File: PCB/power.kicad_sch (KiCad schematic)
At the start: 59 parts, among them CON1 AVR-JTAG-10, U1 LM3880, U2 LM3880, U20 xc7z020clg484, U3 SC189 - 1.0V, U4 SC189 - 3.3V, U5 TLV62080DSGx, U7 SC189 - 1.8V

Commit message: Resolved most of the errors
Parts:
- added J401: Conn_01x02, Connector_PinSocket_1.00mm:PinSocket_1x02_P1.00mm_Vertical, symbol Connector_Generic:Conn_01x02
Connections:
- net +5V: now also J401.1 (Pin_1)
- net GND: now also J401.2 (Pin_2)
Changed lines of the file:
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@@
+	(symbol
+		(lib_id "DFTBoard-rescue:+5V-power")
+		(at 153.67 52.07 0)
+		(unit 1)
+		(exclude_from_sim no)
+		(in_bom yes)
+		(on_board yes)
+		(dnp no)
+		(property "Reference" "#PWR0402"
+			(at 153.67 49.784 0)
+			(effects
+				(font
+					(size 0.508 0.508)
+				)
+				(hide yes)
+			)
+		)
+		(property "Value" "+5V"
+			(at 153.67 49.784 0)
+			(effects
+				(font
+					(size 0.762 0.762)
+				)
+			)
+		)
+		(property "Footprint" ""
+			(at 153.67 52.07 0)
+			(effects
+				(font
+					(size 1.524 1.524)
+				)
+				(hide yes)
+			)
+		)
+		(property "Datasheet" ""
+			(at 153.67 52.07 0)
+			(effects
+				(font
+					(size 1.524 1.524)
+				)
+				(hide yes)
+			)
+		)
+		(property "Description" ""
+			(at 153.67 52.07 0)
+			(effects
+				(font
+					(size 1.27 1.27)
+				)
+				(hide yes)
+			)
+		)
+		(pin "1"
+		)
+		(instances
+			(project "DFTBoard"
+				(path "/0cf42e13-7c72-4f5f-898b-a3f851b94890/00000000-0000-0000-0000-000058508414"
+					(reference "#PWR0402")
+					(unit 1)
+				)
+			)
+		)
+	)
 	(symbol
 		(lib_id "DFTBoard-rescue:+5V-power")
@@
 					(unit 1)
 				)
+			)
+		)
+	)
+	(symbol
+		(lib_id "DFTBoard-rescue:GND-power")
+		(at 153.67 54.61 0)
+		(unit 1)
+		(exclude_from_sim no)
+		(in_bom yes)
+		(on_board yes)
+		(dnp no)
+		(property "Reference" "#PWR0403"
+			(at 153.67 54.61 0)
+			(effects
+				(font
+					(size 0.762 0.762)
+				)
+				(hide yes)
+			)
+		)
+		(property "Value" "GND"
+			(at 153.67 56.388 0)
+			(effects
+				(font
+					(size 0.762 0.762)
+				)
+				(hide yes)
+			)
+		)
+		(property "Footprint" ""
+			(at 153.67 54.61 0)
+			(effects
+				(font
+					(size 1.524 1.524)
+				)
+				(hide yes)
+			)
+		)
+		(property "Datasheet" ""
+			(at 153.67 54.61 0)
+			(effects
+				(font
+					(size 1.524 1.524)
+				)
+				(hide yes)
+			)
+		)
+		(property "Description" ""
+			(at 153.67 54.61 0)
+			(effects
+				(font
+					(size 1.27 1.27)
+				)
+				(hide yes)
+			)
+		)
+		(pin "1"
+		)
+		(instances
+			(project "DFTBoard"
+				(path "/0cf42e13-7c72-4f5f-898b-a3f851b94890/00000000-0000-0000-0000-000058508414"
+					(reference "#PWR0403")
+					(unit 1)
+				)
+			)
+		)
+	)
+	(symbol
+		(lib_id "Connector_Generic:Conn_01x02")
+		(at 158.75 52.07 0)
+		(unit 1)
+		(exclude_from_sim no)
+		(in_bom yes)
+		(on_board yes)
+		(dnp no)
+		(fields_autoplaced yes)
+		(property "Reference" "J401"
+			(at 161.29 52.0699 0)
+			(effects
+				(font
+					(size 1.27 1.27)
+				)
+				(justify left)
+			)
+		)
+		(property "Value" "Conn_01x02"
+			(at 161.29 54.6099 0)
+			(effects
+				(font
+					(size 1.27 1.27)
+				)
+				(justify left)
+			)
+		)
+		(property "Footprint" "Connector_PinSocket_1.00mm:PinSocket_1x02_P1.00mm_Vertical"
+			(at 158.75 52.07 0)
+			(effects
+				(font
+					(size 1.27 1.27)
+				)
+				(hide yes)
+			)
+		)
+		(property "Datasheet" "~"
+			(at 158.75 52.07 0)
+			(effects
+				(font
+					(size 1.27 1.27)
+				)
+				(hide yes)
+			)
+		)
+		(property "Description" "Generic connector, single row, 01x02, script generated (kicad-library-utils/schlib/autogen/connector/)"
+			(at 158.75 52.07 0)
+			(effects
+				(font
+					(size 1.27 1.27)
+				)
+				(hide yes)
+			)
+		)
+		(pin "2"
+		)
+		(pin "1"
+		)
+		(instances
+			(project ""
+				(path "/0cf42e13-7c72-4f5f-898b-a3f851b94890/00000000-0000-0000-0000-000058508414"
+					(reference "J401")
+					(unit 1)
+				)

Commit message: [+] complete PCB design
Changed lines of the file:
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@@
 	)
 	(junction
+		(at 153.67 52.07)
+		(diameter 0)
+		(color 0 0 0 0)
+	)
+	(junction
 		(at 118.11 152.4)
 		(diameter 0)
@@
 	(wire
 		(pts
+			(xy 151.13 52.07) (xy 153.67 52.07)
+		)
+		(stroke
+			(width 0)
+			(type default)
+		)
+	)
+	(wire
+		(pts
 			(xy 237.49 97.79) (xy 237.49 99.06)
 		)
@@
 	(symbol
 		(lib_id "DFTBoard-rescue:+5V-power")
-		(at 153.67 52.07 0)
+		(at 151.13 52.07 0)
 		(unit 1)
 		(exclude_from_sim no)
@@
 		(dnp no)
 		(property "Reference" "#PWR0402"
-			(at 153.67 49.784 0)
+			(at 151.13 49.784 0)
 			(effects
 				(font
@@
 		)
 		(property "Value" "+5V"
-			(at 153.67 49.784 0)
+			(at 151.13 49.784 0)
 			(effects
 				(font
@@
 		)
 		(property "Footprint" ""
-			(at 153.67 52.07 0)
+			(at 151.13 52.07 0)
 			(effects
 				(font
@@
 		)
 		(property "Datasheet" ""
-			(at 153.67 52.07 0)
+			(at 151.13 52.07 0)
 			(effects
 				(font
@@
 		)
 		(property "Description" ""
-			(at 153.67 52.07 0)
+			(at 151.13 52.07 0)
 			(effects
 				(font
@@
 					(unit 1)
 				)
+			)
+		)
+	)
+	(symbol
+		(lib_id "DFTBoard-rescue:PWR_FLAG")
+		(at 153.67 52.07 0)
+		(unit 1)
+		(exclude_from_sim no)
+		(in_bom yes)
+		(on_board yes)
+		(dnp no)
+		(property "Reference" "#FLG0401"
+			(at 153.67 50.165 0)
+			(effects
+				(font
+					(size 1.27 1.27)
+				)
+				(hide yes)
+			)
+		)
+		(property "Value" "PWR_FLAG"
+			(at 153.67 48.8188 90)
+			(effects
+				(font
+					(size 1.27 1.27)
+				)
+				(justify left)
+			)
+		)
+		(property "Footprint" ""
+			(at 153.67 52.07 0)
+			(effects
+				(font
+					(size 1.27 1.27)
+				)
+				(hide yes)
+			)
+		)
+		(property "Datasheet" ""
+			(at 153.67 52.07 0)
+			(effects
+				(font
+					(size 1.27 1.27)
+				)
+				(hide yes)
+			)
+		)
+		(property "Description" ""
+			(at 153.67 52.07 0)
+			(effects
+				(font
+					(size 1.27 1.27)
+				)
+				(hide yes)
+			)
+		)
+		(pin "1"
+		)
+		(instances
+			(project "DFTBoard"
+				(path "/0cf42e13-7c72-4f5f-898b-a3f851b94890/00000000-0000-0000-0000-000058508414"
+					(reference "#FLG0401")
+					(unit 1)
+				)

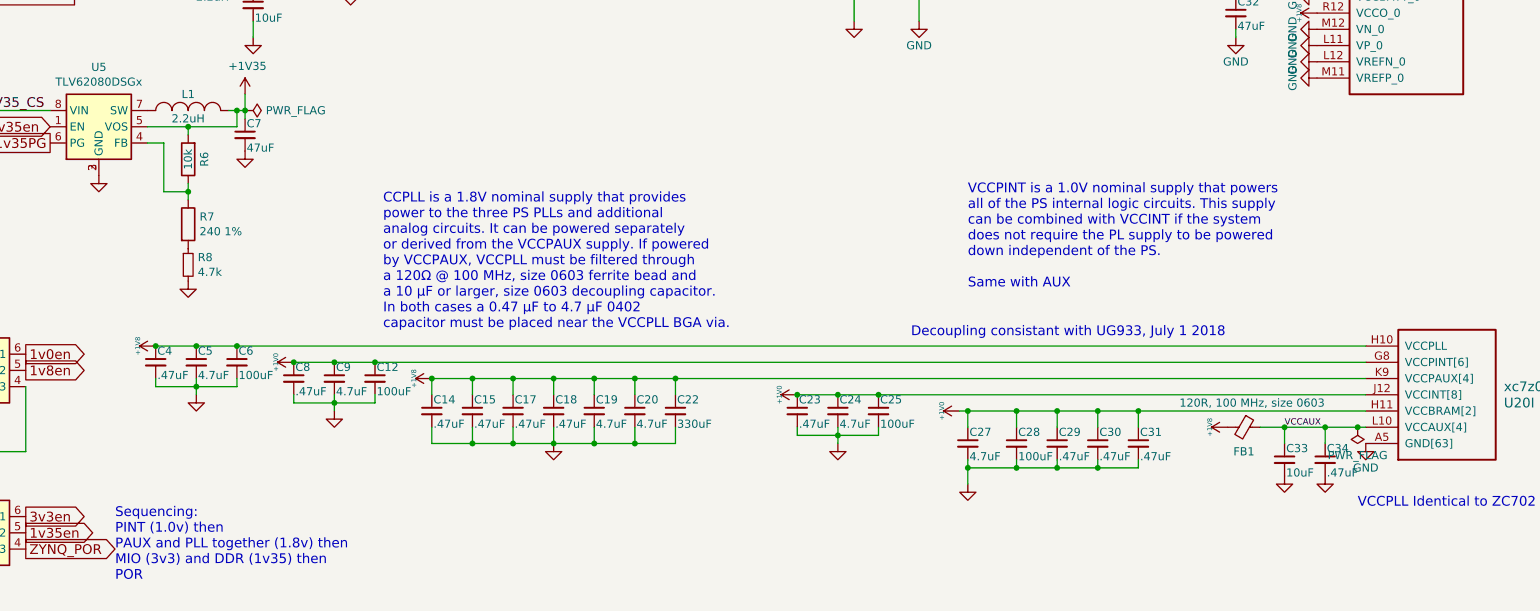
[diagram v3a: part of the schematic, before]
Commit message: [+] add XDC files
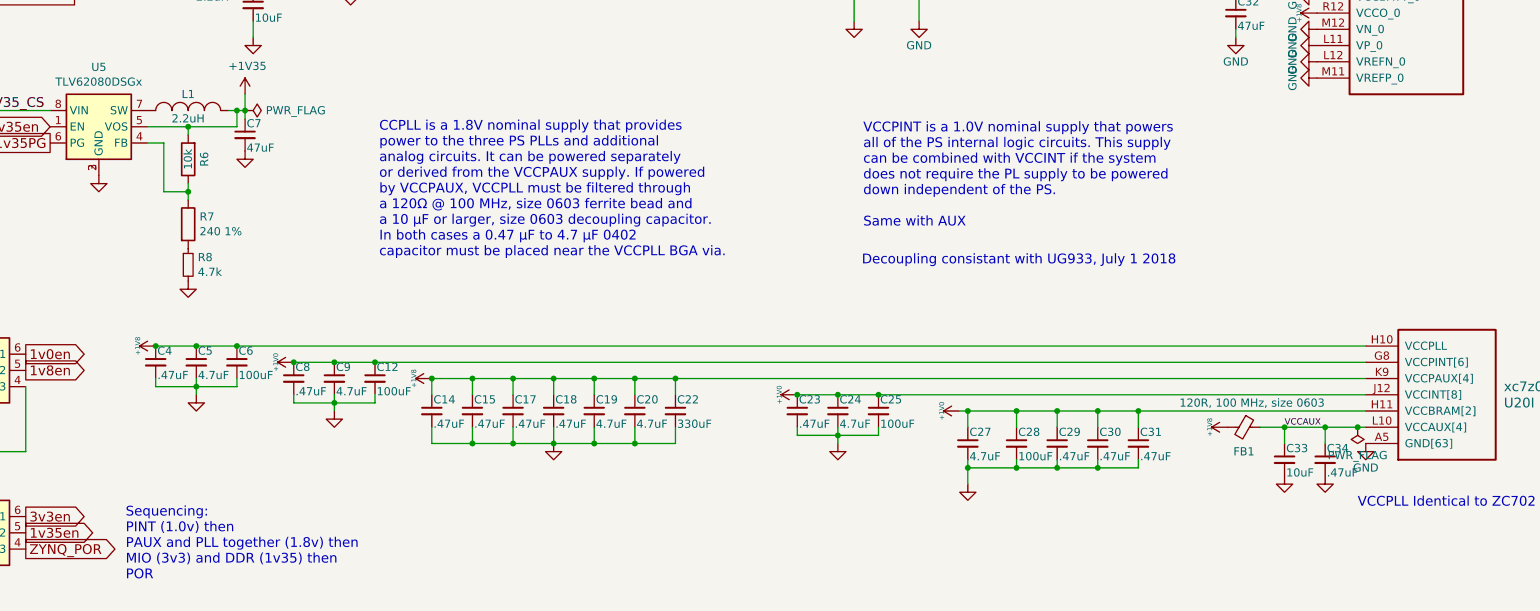
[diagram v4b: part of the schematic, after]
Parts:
- J401: footprint Connector_PinSocket_1.00mm:PinSocket_1x02_P1.00mm_Vertical -> Phoenix_custom:PHOENIX_1748167
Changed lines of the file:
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@@
 	(text "Decoupling consistant with UG933, July 1 2018"
 		(exclude_from_sim no)
-		(at 186.69 146.05 0)
+		(at 178.9938 134.8232 0)
 		(effects
 			(font
@@
 	(text "CCPLL is a 1.8V nominal supply that provides \npower to the three PS PLLs and additional\nanalog circuits. It can be powered separately \nor derived from the VCCPAUX supply. If powered\nby VCCPAUX, VCCPLL must be filtered through \na 120Ω @ 100 MHz, size 0603 ferrite bead and\na 10 µF or larger, size 0603 decoupling capacitor. \nIn both cases a 0.47 µF to 4.7 µF 0402\ncapacitor must be placed near the VCCPLL BGA via. "
 		(exclude_from_sim no)
-		(at 104.14 144.78 0)
+		(at 103.5304 133.5532 0)
 		(effects
 			(font
@@
 	(text "VCCPINT is a 1.0V nominal supply that powers \nall of the PS internal logic circuits. This supply \ncan be combined with VCCINT if the system \ndoes not require the PL supply to be powered \ndown independent of the PS.\n\nSame with AUX"
 		(exclude_from_sim no)
-		(at 195.58 138.43 0)
+		(at 179.2224 128.905 0)
 		(effects
 			(font
@@
 	(text "Sequencing: \nPINT (1.0v) then \nPAUX and PLL together (1.8v) then\nMIO (3v3) and DDR (1v35) then\nPOR"
 		(exclude_from_sim no)
-		(at 62.23 184.15 0)
+		(at 63.881 184.0738 0)
 		(effects
 			(font
@@
 			)
 		)
-		(property "Footprint" "Connector_PinSocket_1.00mm:PinSocket_1x02_P1.00mm_Vertical"
+		(property "Footprint" "Phoenix_custom:PHOENIX_1748167"
 			(at 158.75 52.07 0)
 			(effects
